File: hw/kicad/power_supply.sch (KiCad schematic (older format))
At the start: 28 parts

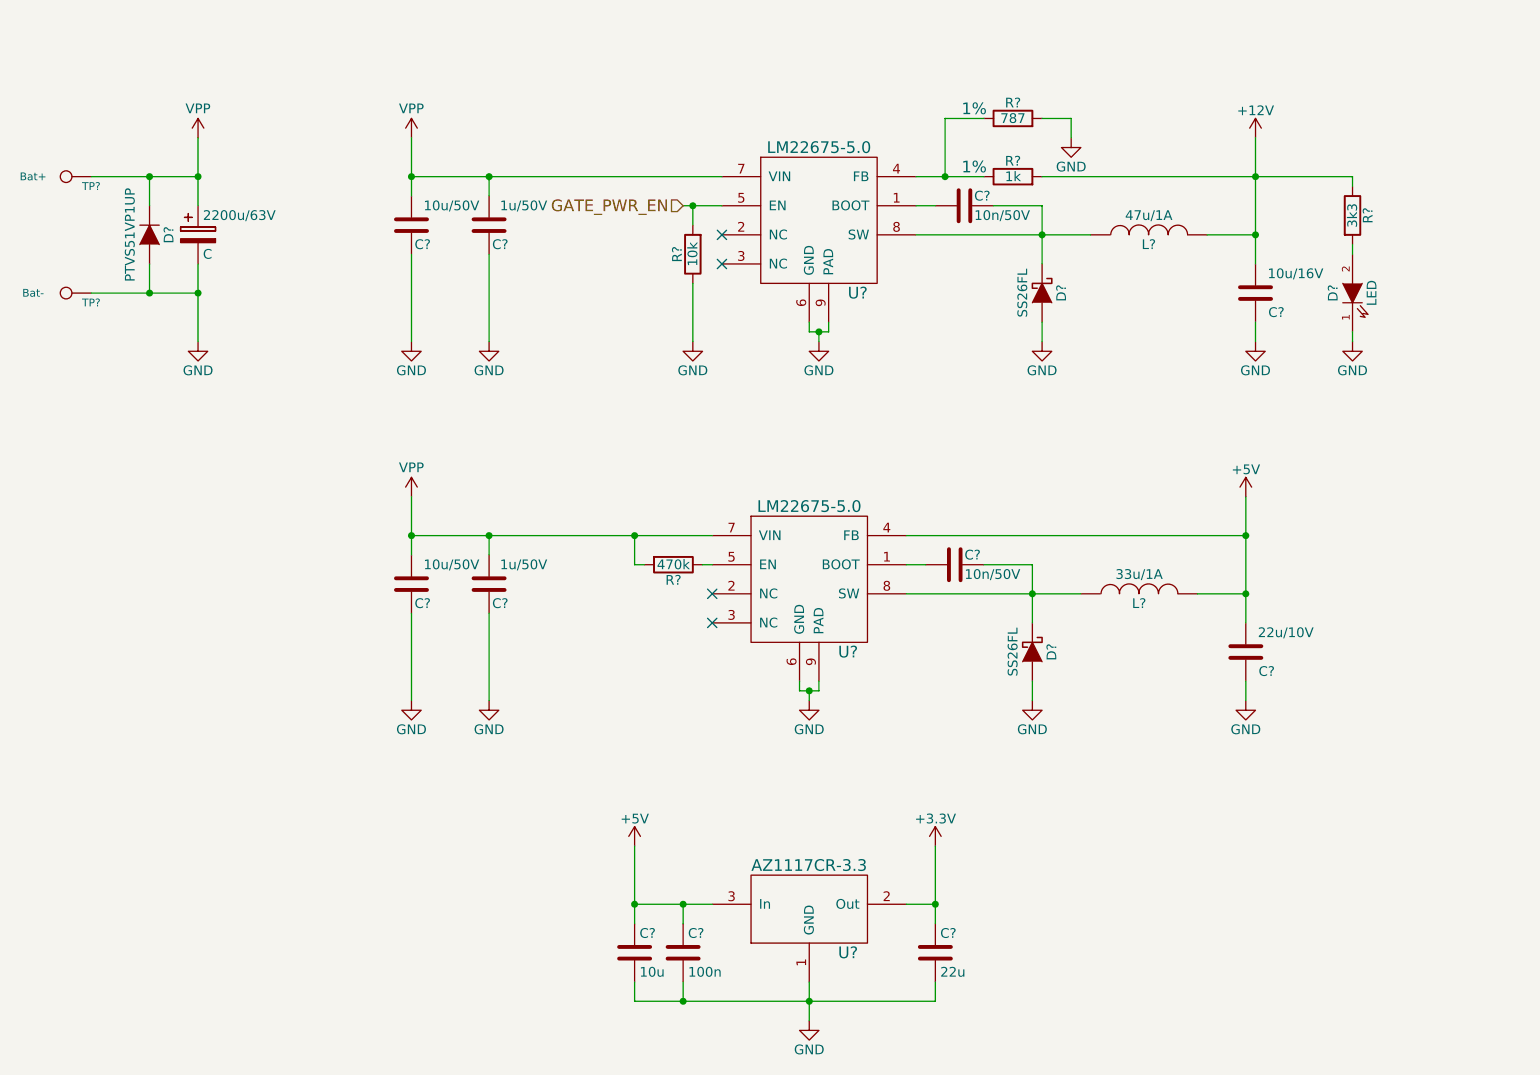
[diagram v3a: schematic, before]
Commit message: TVS on 5V and 3.3V rails
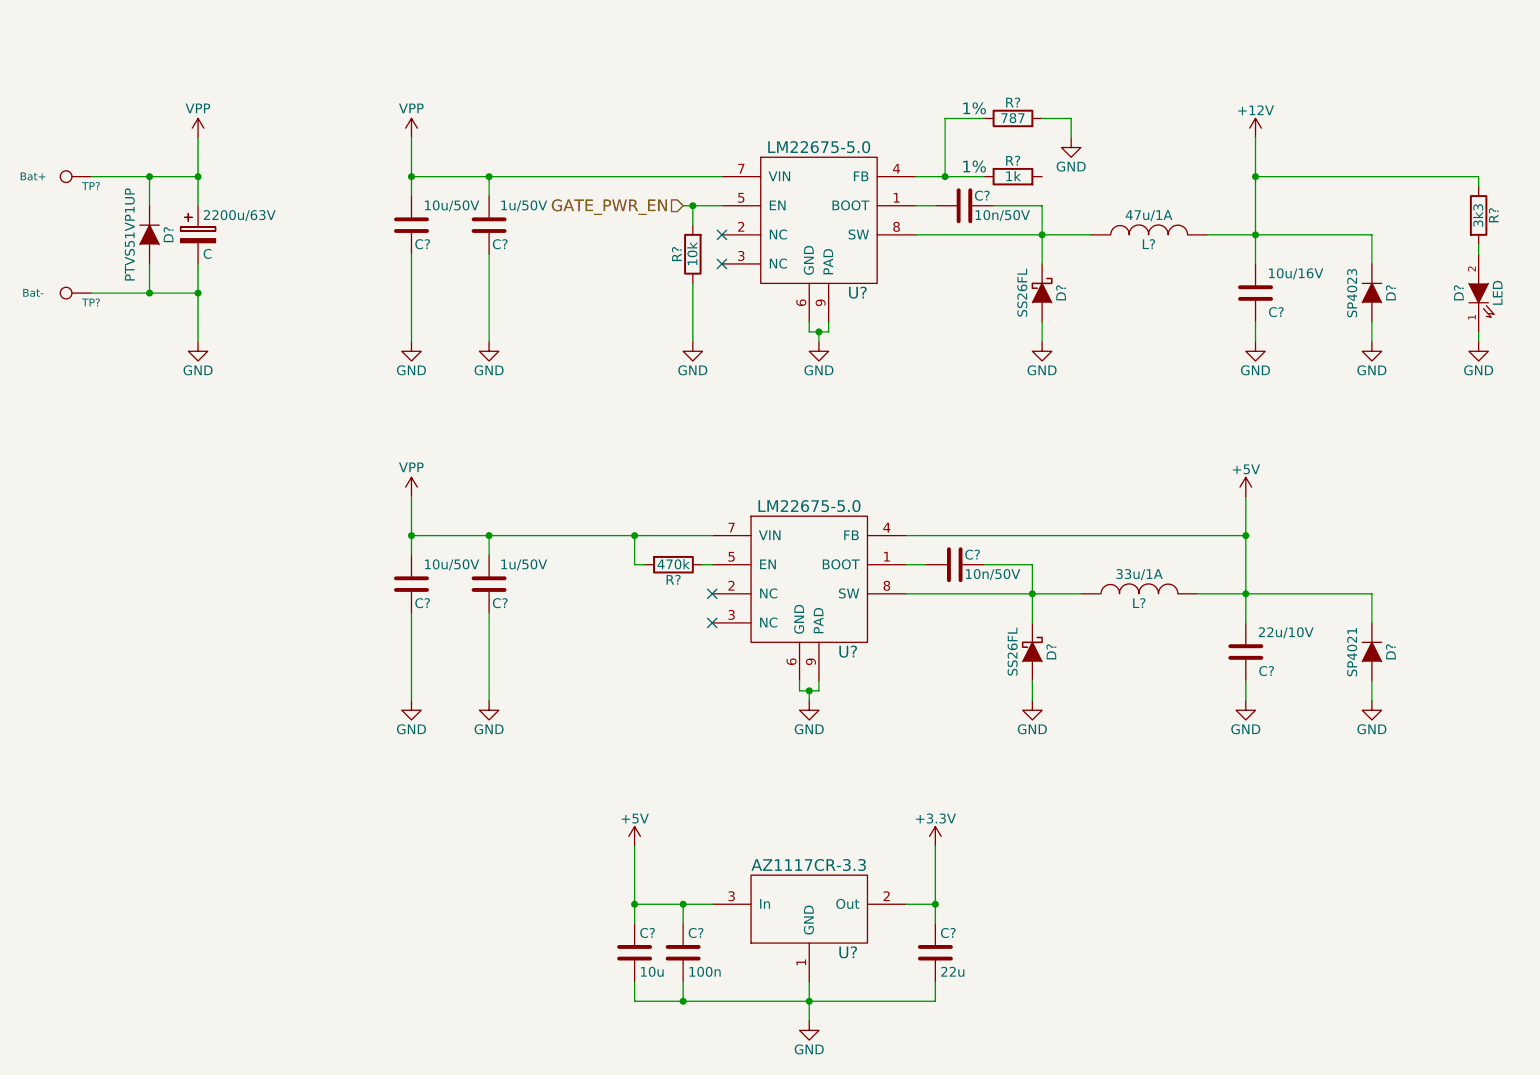
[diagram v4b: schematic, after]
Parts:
- added D?: SP4023, Diodes_SMD:SOD-323, symbol D
- added D?: SP4021, Diodes_SMD:SOD-323, symbol D
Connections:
- net +12V: now also D?.1 (K); no longer R?.2
- net +5V: now also D?.1 (K)
- net GND: now also D?.2 (A), D?.2 (A)
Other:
- moved on the sheet: D?, R?
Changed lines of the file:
@@
 	4750 5600 4750 5500
 Wire Wire Line
-	4500 5500 4750 5500
-Wire Wire Line
-	4750 5500 4900 5500
+	4500 5500 4900 5500
 Wire Wire Line
 	5900 5500 6050 5500
 Wire Wire Line
-	6050 5200 6050 5500
-Wire Wire Line
-	6050 5500 6050 5600
-Wire Wire Line
-	5400 5900 5400 6000
-Wire Wire Line
-	5400 6000 5400 6100
-Wire Wire Line
-	4500 6000 4750 6000
-Wire Wire Line
-	4750 6000 5400 6000
-Wire Wire Line
-	5400 6000 6050 6000
+	6050 5200 6050 5600
+Wire Wire Line
+	5400 5900 5400 6100
+Wire Wire Line
+	4500 6000 6050 6000
 Wire Wire Line
 	6050 6000 6050 5900
@@
 Connection ~ 4750 6000
 Wire Wire Line
-	4500 5200 4500 5500
-Wire Wire Line
-	4500 5500 4500 5600
+	4500 5200 4500 5600
 Connection ~ 4750 5500
 Connection ~ 4500 5500
@@
 $EndComp
 Wire Wire Line
-	2250 2600 2250 2350
-Wire Wire Line
-	2250 2350 2250 2200
-Wire Wire Line
-	2250 1900 2250 1750
-Wire Wire Line
-	2250 1750 2250 1550
+	2250 2200 2250 2600
+Wire Wire Line
+	2250 1550 2250 1900
 $Comp
 L GND #PWR?
@@
 	5400 2500 5400 2550
 Wire Wire Line
-	5400 2550 5450 2550
-Wire Wire Line
-	5450 2550 5500 2550
+	5400 2550 5500 2550
 Wire Wire Line
 	5450 2550 5450 2600
@@
 $EndComp
 Wire Wire Line
-	5950 1750 6100 1750
-Wire Wire Line
-	6100 1750 6300 1750
+	5950 1750 6300 1750
 Wire Wire Line
 	6300 1450 6100 1450
@@
 	5950 1900 6050 1900
 Wire Wire Line
-	5950 2050 6600 2050
-Wire Wire Line
-	6600 2050 6850 2050
-Wire Wire Line
-	6600 1900 6600 2050
-Wire Wire Line
-	6600 2050 6600 2200
+	5950 2050 6850 2050
+Wire Wire Line
+	6600 1900 6600 2200
 Wire Wire Line
 	6600 1900 6350 1900
@@
 $EndComp
 Wire Wire Line
-	7700 2050 7450 2050
-Wire Wire Line
-	7700 1550 7700 1750
-Wire Wire Line
-	7700 1750 7700 2050
-Wire Wire Line
-	7700 2050 7700 2200
+	7450 2050 8300 2050
+Wire Wire Line
+	7700 1550 7700 2200
 $Comp
 L GND #PWR?
@@
 	7700 2600 7700 2500
 Wire Wire Line
-	6600 1750 7700 1750
-Wire Wire Line
-	7700 1750 8200 1750
+	7700 1750 8850 1750
 Connection ~ 7700 2050
 $Comp
@@
 	3750 1850 3750 1750
 Wire Wire Line
-	3350 1750 3750 1750
-Wire Wire Line
-	3750 1750 4950 1750
+	3350 1750 4950 1750
 $Comp
 L C C?
@@
 $EndComp
 Wire Wire Line
-	3350 1550 3350 1750
-Wire Wire Line
-	3350 1750 3350 1850
+	3350 1550 3350 1850
 Connection ~ 3750 1750
 $Comp
@@
 L LED D?
 U 1 1 5830FEC8
-P 8200 2350
-F 0 "D?" H 8200 2450 50  0000 C CNN
-F 1 "LED" H 8200 2250 50  0000 C CNN
-F 2 "" H 8200 2350 60  0000 C CNN
-F 3 "" H 8200 2350 60  0000 C CNN
-	1    8200 2350
+P 8850 2350
+F 0 "D?" H 8850 2450 50  0000 C CNN
+F 1 "LED" H 8850 2250 50  0000 C CNN
+F 2 "" H 8850 2350 60  0000 C CNN
+F 3 "" H 8850 2350 60  0000 C CNN
+	1    8850 2350
 	0    -1   -1   0
 $EndComp
@@
 L GND #PWR?
 U 1 1 5830FFA0
-P 8200 2600
-F 0 "#PWR?" H 8200 2350 50  0001 C CNN
-F 1 "GND" H 8200 2450 50  0000 C CNN
-F 2 "" H 8200 2600 60  0000 C CNN
-F 3 "" H 8200 2600 60  0000 C CNN
-	1    8200 2600
-	1    0    0    -1
-$EndComp
-Wire Wire Line
-	8200 2600 8200 2550
+P 8850 2600
+F 0 "#PWR?" H 8850 2350 50  0001 C CNN
+F 1 "GND" H 8850 2450 50  0000 C CNN
+F 2 "" H 8850 2600 60  0000 C CNN
+F 3 "" H 8850 2600 60  0000 C CNN
+	1    8850 2600
+	1    0    0    -1
+$EndComp
+Wire Wire Line
+	8850 2600 8850 2550
 $Comp
 L R R?
 U 1 1 58310060
-P 8200 1950
-F 0 "R?" V 8280 1950 50  0000 C CNN
-F 1 "3k3" V 8200 1950 50  0000 C CNN
-F 2 "" V 8130 1950 30  0000 C CNN
-F 3 "" H 8200 1950 30  0000 C CNN
-	1    8200 1950
-	1    0    0    -1
-$EndComp
-Wire Wire Line
-	8200 1750 8200 1800
-Wire Wire Line
-	8200 2150 8200 2100
+P 8850 1950
+F 0 "R?" V 8930 1950 50  0000 C CNN
+F 1 "3k3" V 8850 1950 50  0000 C CNN
+F 2 "" V 8780 1950 30  0000 C CNN
+F 3 "" H 8850 1950 30  0000 C CNN
+	1    8850 1950
+	1    0    0    -1
+$EndComp
+Wire Wire Line
+	8850 1750 8850 1800
+Wire Wire Line
+	8850 2150 8850 2100
 $Comp
 L GND #PWR?
@@
 	5350 4350 5350 4400
 Wire Wire Line
-	5350 4400 5400 4400
-Wire Wire Line
-	5400 4400 5450 4400
+	5350 4400 5450 4400
 Wire Wire Line
 	5400 4400 5400 4450
@@
 	5900 3750 6000 3750
 Wire Wire Line
-	5900 3900 6550 3900
-Wire Wire Line
-	6550 3900 6800 3900
-Wire Wire Line
-	6550 3750 6550 3900
-Wire Wire Line
-	6550 3900 6550 4050
+	5900 3900 6800 3900
+Wire Wire Line
+	6550 3750 6550 4050
 Wire Wire Line
 	6550 3750 6300 3750
@@
 $EndComp
 Wire Wire Line
-	7650 3900 7400 3900
-Wire Wire Line
-	7650 3400 7650 3600
-Wire Wire Line
-	7650 3600 7650 3900
-Wire Wire Line
-	7650 3900 7650 4050
+	7400 3900 8300 3900
+Wire Wire Line
+	7650 3400 7650 4050
 $Comp
 L GND #PWR?
@@
 	3750 3700 3750 3600
 Wire Wire Line
-	3350 3600 3750 3600
-Wire Wire Line
-	3750 3600 4500 3600
-Wire Wire Line
-	4500 3600 4900 3600
+	3350 3600 4900 3600
 $Comp
 L C C?
@@
 $EndComp
 Wire Wire Line
-	3350 3400 3350 3600
-Wire Wire Line
-	3350 3600 3350 3700
+	3350 3400 3350 3700
 Connection ~ 3750 3600
 $Comp
@@
 GATE_PWR_EN
 Wire Wire Line
-	4750 1900 4800 1900
-Wire Wire Line
-	4800 1900 4950 1900
+	4750 1900 4950 1900
 $Comp
 L R R?
@@
 $EndComp
 Wire Wire Line
-	1700 2350 2000 2350
-Wire Wire Line
-	2000 2350 2250 2350
+	1700 2350 2250 2350
 Wire Wire Line
 	2000 2350 2000 2200
@@
 	2000 1900 2000 1750
 Wire Wire Line
-	1700 1750 2000 1750
-Wire Wire Line
-	2000 1750 2250 1750
+	1700 1750 2250 1750
 Connection ~ 2250 2350
 Connection ~ 2000 2350
 Connection ~ 2250 1750
 Connection ~ 2000 1750
+$Comp
+L D D?
+U 1 1 583A11EB
+P 8300 2350
+F 0 "D?" H 8300 2450 50  0000 C CNN
+F 1 "SP4023" H 8300 2250 50  0000 C CNN
+F 2 "Diodes_SMD:SOD-323" H 8300 2350 60  0001 C CNN
+F 3 "" H 8300 2350 60  0000 C CNN
+	1    8300 2350
+	0    1    1    0
+$EndComp
+Wire Wire Line
+	8300 2050 8300 2200
+$Comp
+L GND #PWR?
+U 1 1 583A15DE
+P 8300 2600
+F 0 "#PWR?" H 8300 2350 50  0001 C CNN
+F 1 "GND" H 8300 2450 50  0000 C CNN
+F 2 "" H 8300 2600 60  0000 C CNN
+F 3 "" H 8300 2600 60  0000 C CNN
+	1    8300 2600
+	1    0    0    -1
+$EndComp
+Wire Wire Line
+	8300 2600 8300 2500
+$Comp
+L D D?
+U 1 1 583A1F54
+P 8300 4200
+F 0 "D?" H 8300 4300 50  0000 C CNN
+F 1 "SP4021" H 8300 4100 50  0000 C CNN
+F 2 "Diodes_SMD:SOD-323" H 8300 4200 60  0001 C CNN
+F 3 "" H 8300 4200 60  0000 C CNN
+	1    8300 4200
+	0    1    1    0
+$EndComp
+Wire Wire Line
+	8300 3900 8300 4050
+$Comp
+L GND #PWR?
+U 1 1 583A21F7
+P 8300 4450
+F 0 "#PWR?" H 8300 4200 50  0001 C CNN
+F 1 "GND" H 8300 4300 50  0000 C CNN
+F 2 "" H 8300 4450 60  0000 C CNN
+F 3 "" H 8300 4450 60  0000 C CNN
+	1    8300 4450
+	1    0    0    -1
+$EndComp
+Wire Wire Line
+	8300 4450 8300 4350
 $EndSCHEMATC

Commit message: Annotation
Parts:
- C52: renamed from 2200u/63V; value C -> 2200u/63V1
- gave numbers to parts that had none: 29

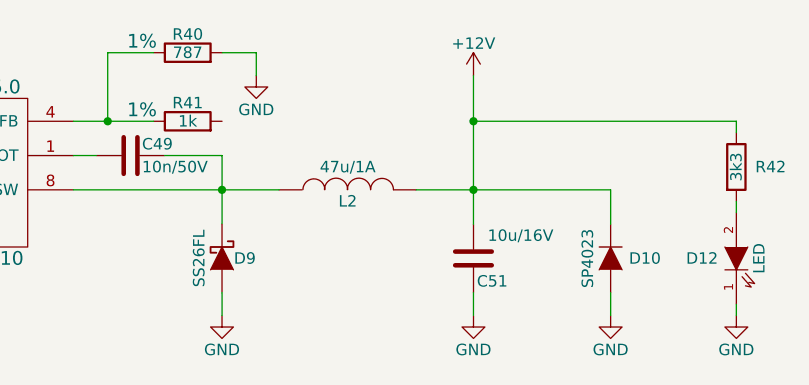
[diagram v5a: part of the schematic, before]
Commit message: Map footprints to components and add BOM
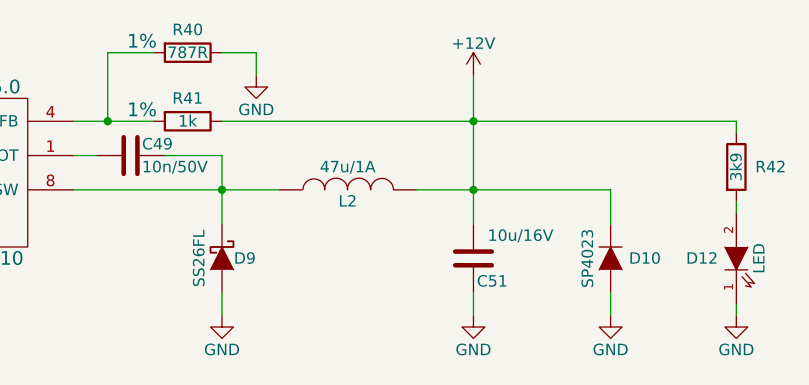
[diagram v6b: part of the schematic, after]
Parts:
- C41, C42: footprint (none) -> Capacitors_SMD:C_1210
- C43, C44, C45, C47, C50, C51: footprint (none) -> Capacitors_SMD:C_0805
- C46, C48, C49: footprint (none) -> Capacitors_SMD:C_0402
- C52: footprint (none) -> Capacitors_ThroughHole:C_Radial_D18_L36_P7.5
- D12: footprint (none) -> LEDs:LED_0603
- L1, L2: footprint (none) -> SRN8040TA:SRN8040TA
- R38, R39: footprint (none) -> Resistors_SMD:R_0402
- R40: value 787 -> 787R; footprint (none) -> Resistors_SMD:R_0402;  Tolerance (none) -> 1%; Prec 1% -> (none)
- R41: footprint (none) -> Resistors_SMD:R_0402;  Tolerance (none) -> 1%; Prec 1% -> (none)
- R42: value 3k3 -> 3k9; footprint (none) -> Resistors_SMD:R_0402
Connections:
- net +12V: now also R41.1
- net GND: now also R40.1; no longer R40.2
- net at R41.2: now also R40.2, U10.4 (FB)

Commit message: Aligned, started rework current shunt layout and copper pour
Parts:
- TP4, TP5: footprint Wire_Pads:SolderWirePad_single_SMD_5x10mm -> pads:SolderWirePad_single_SMD_5x5mm
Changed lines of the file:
@@
 F 0 "TP4" V 1600 1700 40  0000 C CNN
 F 1 "Bat+" V 1650 2000 40  0000 C CNN
-F 2 "Wire_Pads:SolderWirePad_single_SMD_5x10mm" V 1650 1900 60  0001 C CNN
+F 2 "pads:SolderWirePad_single_SMD_5x5mm" V 1650 1900 60  0001 C CNN
 F 3 "" V 1650 1900 60  0000 C CNN
 	1    1650 1750
@@
 F 0 "TP5" V 1600 2300 40  0000 C CNN
 F 1 "Bat-" V 1650 2600 40  0000 C CNN
-F 2 "Wire_Pads:SolderWirePad_single_SMD_5x10mm" V 1650 2500 60  0001 C CNN
+F 2 "pads:SolderWirePad_single_SMD_5x5mm" V 1650 2500 60  0001 C CNN
 F 3 "" V 1650 2500 60  0000 C CNN
 	1    1650 2350
